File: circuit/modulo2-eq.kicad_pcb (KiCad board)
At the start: 2 copper layers, 63 parts, among them J1 JACK_MONO, J2 HOLE, J3 HOLE, J4 CONN_01X04, J5 CONN_01X02, Q1 MMBFJ201, U1 NE5532, U2 NE5532, U3 NE5532, U4 NE5532, U5 TLE2426

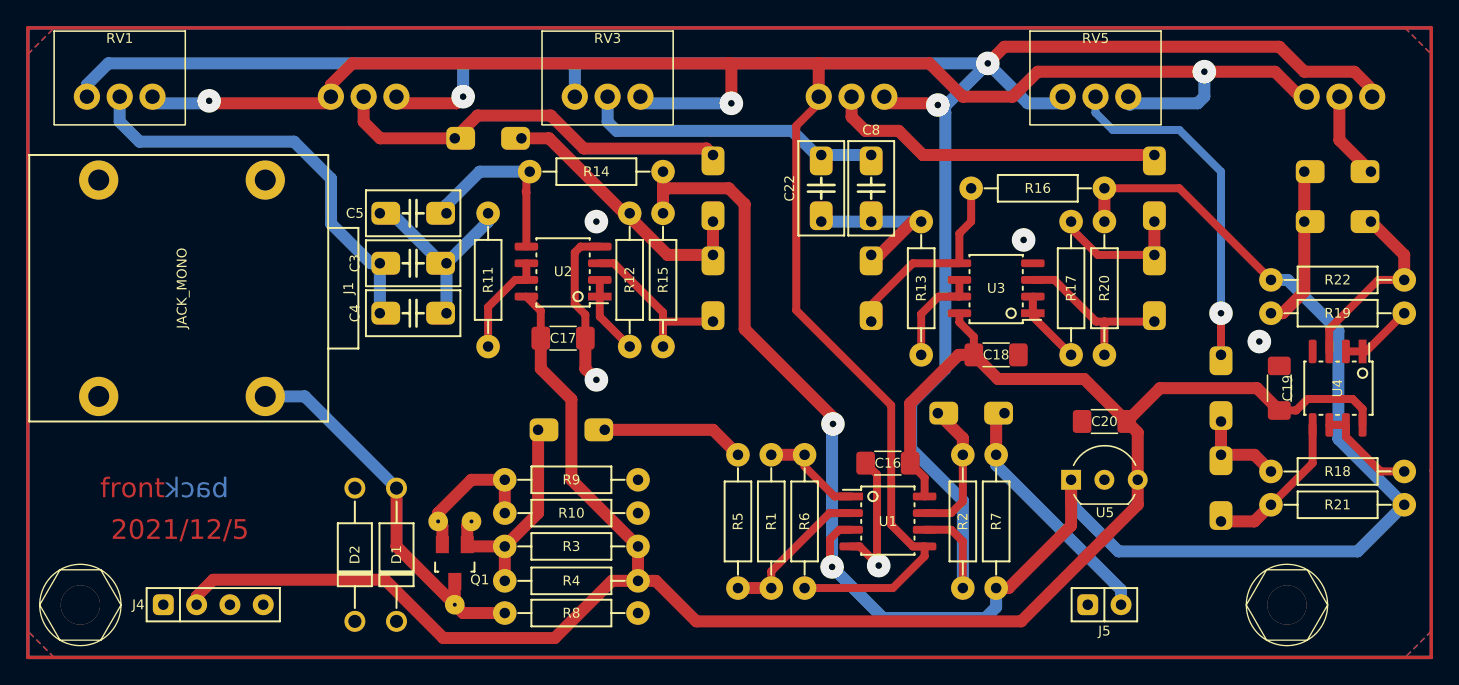
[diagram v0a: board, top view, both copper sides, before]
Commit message: found new switch for gain select; eq needs redesign
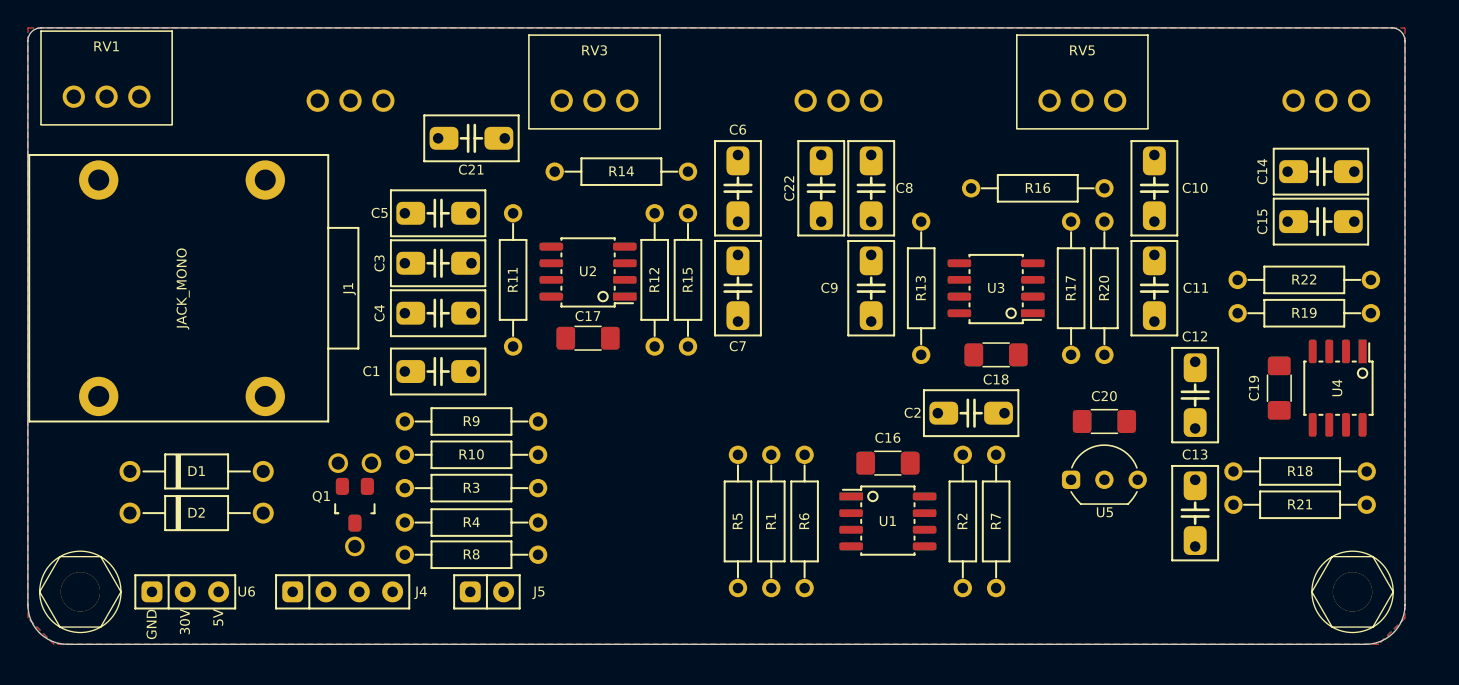
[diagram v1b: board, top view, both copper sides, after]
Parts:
- added U6: PWR_CONN, myAmp:PWR_CONN, F.Cu at (62.0, 93.0)
- C1, C10, C11, C12, C13, C14, C15, C2, C21, C6, C7, C9: moved to F.Cu
- D1, D2: value 1N4773a -> 1N4733a
- R1, R10, R11, R12, R13, R14, R15, R16, R17, R18, R19, R2, R20, R21, R22, R3, R4, R5, R6, R7, R8, R9: footprint myAmp:R_10MM_TT -> myAmp:R_10MM
- moved J5 47.1 mm to (85.0, 93.0)
- moved D1 16.5 mm to (62.9, 83.8), turned to 0 degrees
- moved D2 12.5 mm to (62.9, 87.0), turned to 0 degrees
- moved C1 11.1 mm to (81.3, 76.2)
- moved J4 9.91 mm to (74.0, 93.0)
- moved R10 8.82 mm to (83.8, 82.5)
- moved R4 8.82 mm to (83.8, 87.7)
- moved R3 8.82 mm to (83.8, 85.1)
- moved R8 8.82 mm to (83.8, 90.2)
- moved R9 8.82 mm to (83.8, 80.0)
- moved Q1 8.82 mm to (74.9, 86.4)
- moved J2 5.10 mm to (151.0, 93.0)
- moved R18 2.86 mm to (147.0, 83.8)
- moved R21 2.86 mm to (147.0, 86.4)
- moved C13 2.74 mm to (139.0, 87.0)
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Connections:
- J2 pad 1: (no net) -> unconnected-(J2-Pad1)
- J3 pad 1: (no net) -> unconnected-(J3-Pad1)
- J4 pad 2: +BATT -> /OUT
- J4 pad 3: (no net) -> GND
- J4 pad 4: (no net) -> /OUT
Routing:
- net (no net): track 620.0 -> 0.00 mm
- net BOOST: track 177.2 -> 0.00 mm, vias 3 -> 0
- net +BATT: track 166.4 -> 0.00 mm
- net CUT: track 164.3 -> 0.00 mm, vias 3 -> 0
- net VGND: track 142.7 -> 0.00 mm, vias 2 -> 0
- net Net-(C3-Pad2): track 31.5 -> 0.00 mm
- net Net-(C21-Pad2): track 30.5 -> 0.00 mm
- net /jfet_g: track 29.5 -> 0.00 mm
- net Net-(C12-Pad2): track 26.1 -> 0.00 mm, vias 1 -> 0
- net Net-(C10-Pad2): track 25.3 -> 0.00 mm
- net GND: track 23.4 -> 0.00 mm, vias 5 -> 0
- net Net-(C22-Pad2): track 22.6 -> 0.00 mm
- net Net-(C21-Pad1): track 21.0 -> 0.00 mm
- net /OUT: track 18.8 -> 0.00 mm
- net /jfet_d: track 17.4 -> 0.00 mm
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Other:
- board outline added: 105 x 47 mm
- net class Default removed
- board text removed: "2021/12/5"
- board text removed: "back"
- board text removed: "front"

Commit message: routed eq pcb
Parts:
- removed C2: 1μF, myAmp:C_5MM_1206
- removed R7: 100k, myAmp:R_10MM
- C1, C3: footprint myAmp:C_5MM_1206 -> myAmp:C_FILM_L7.2mm_W5.0mm_P5.00mm
- C10, C12, C8: footprint myAmp:C_5MM_1206 -> myAmp:C_FILM_L7.2mm_W3.5mm_P5.00mm
- C18: footprint myAmp:C_1206 -> myAmp:C_FILM_L7.2mm_W2.5mm_P5.00mm
- C21, C22, C4, C6: footprint myAmp:C_5MM_1206 -> myAmp:C_FILM_L7.2mm_W4.5mm_P5.00mm
- moved D2 83.6 mm to (142.9, 62.9), turned to 180 degrees
- moved D1 82.0 mm to (142.9, 66.0), turned to 180 degrees
- moved J1 81.7 mm to (143.0, 78.7), turned to -90 degrees
- moved Q1 52.2 mm to (126.4, 77.5), turned to 0 degrees
- moved C20 48.9 mm to (83.2, 81.3), turned to -90 degrees
- moved C1 47.3 mm to (127.0, 88.3), turned to 90 degrees
- moved U5 45.9 mm to (86.4, 80.6), turned to -90 degrees
- moved R16 42.6 mm to (85.1, 69.8), turned to 90 degrees
- moved R18 41.3 mm to (108.6, 68.6), turned to -90 degrees
- moved R21 40.0 mm to (111.1, 68.6), turned to 90 degrees
- moved R20 39.7 mm to (92.7, 74.9), turned to 0 degrees
- moved C13 38.6 mm to (111.1, 60.3), turned to 180 degrees
- moved C8 38.1 mm to (76.2, 60.3), turned to 180 degrees
- moved C12 37.4 mm to (104.8, 62.9)
- moved C10 35.6 mm to (100.3, 62.9)
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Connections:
- R2 pad 1: Net-(C2-Pad2) -> /OUT
- U1 pad 7: Net-(C2-Pad2) -> /OUT
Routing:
- net +BATT: track 0.00 -> 160.9 mm
- net BOOST: track 0.00 -> 156.7 mm, vias 0 -> 1
- net CUT: track 0.00 -> 134.5 mm, vias 0 -> 1
- net VGND: track 0.00 -> 55.8 mm
- net Net-(C5-Pad1): track 0.00 -> 41.7 mm
- net /OUT: track 0.00 -> 35.8 mm
- net Net-(C22-Pad2): track 0.00 -> 28.7 mm
- net Net-(C12-Pad2): track 0.00 -> 27.6 mm
- net Net-(C3-Pad2): track 0.00 -> 27.2 mm
- net Net-(C7-Pad1): track 0.00 -> 26.7 mm
- net Net-(R1-Pad2): track 0.00 -> 26.1 mm
- net /jfet_g: track 0.00 -> 23.8 mm
- net Net-(C15-Pad1): track 0.00 -> 21.5 mm
- net Net-(C3-Pad1): track 0.00 -> 20.8 mm
- net Net-(C14-Pad2): track 0.00 -> 20.1 mm
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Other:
- board text added: "GND"
- board text added: "OUT"
